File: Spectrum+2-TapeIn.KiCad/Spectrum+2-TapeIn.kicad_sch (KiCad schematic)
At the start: 15 parts, among them U1 LM358

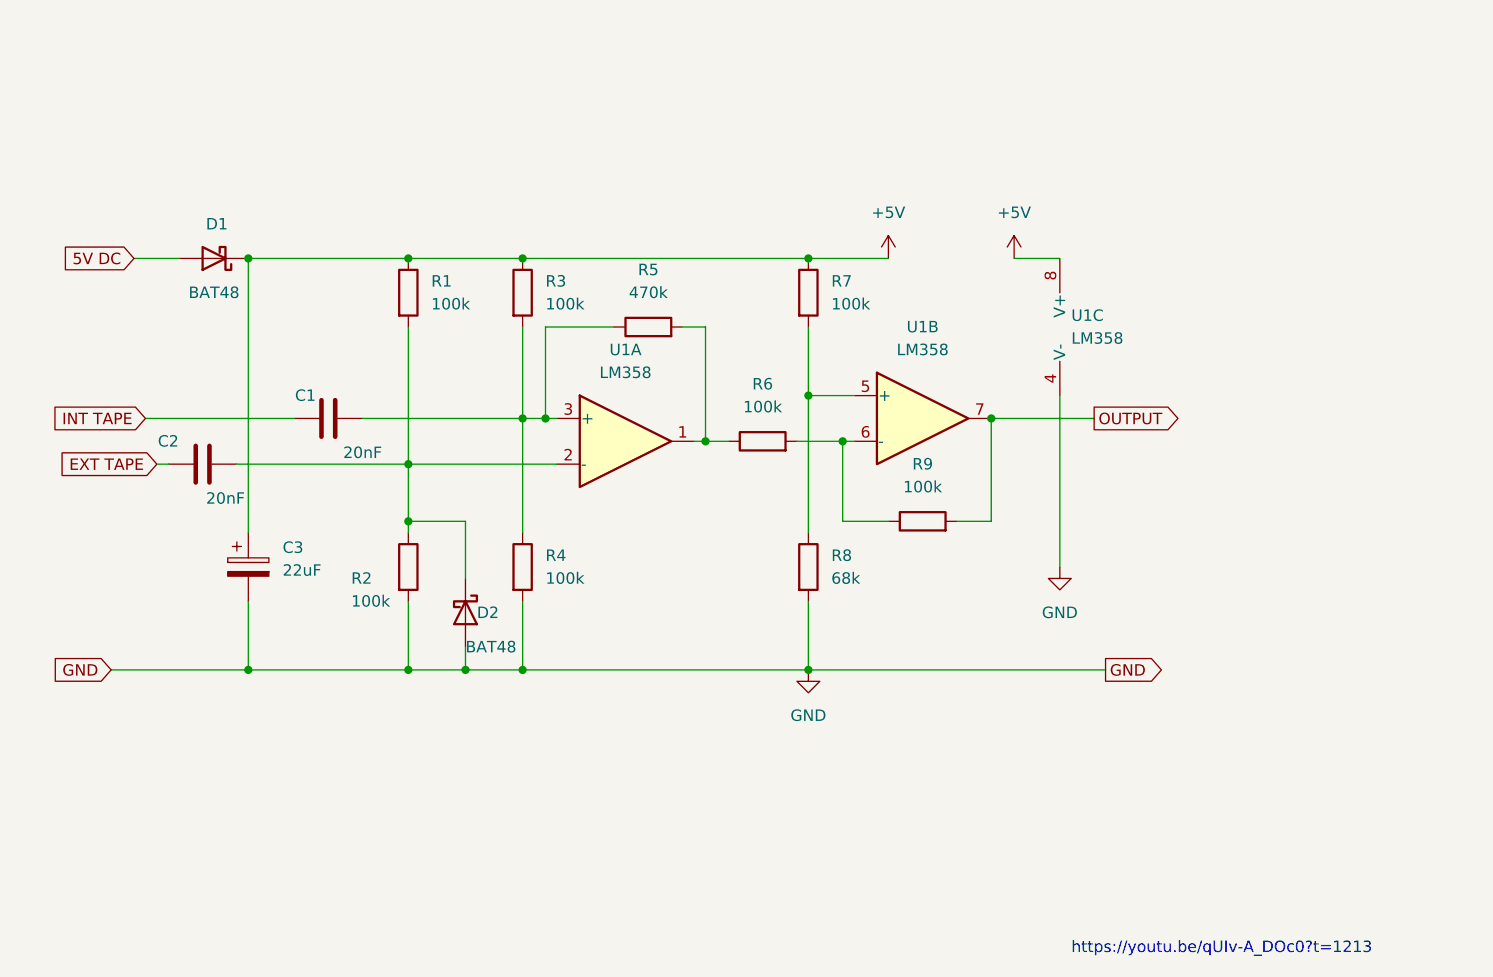
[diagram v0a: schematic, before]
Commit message: Rev. D
Proper connector for deck plug (no need to cut the wires).
Improved silkscreen, makes it easier to place components when building.
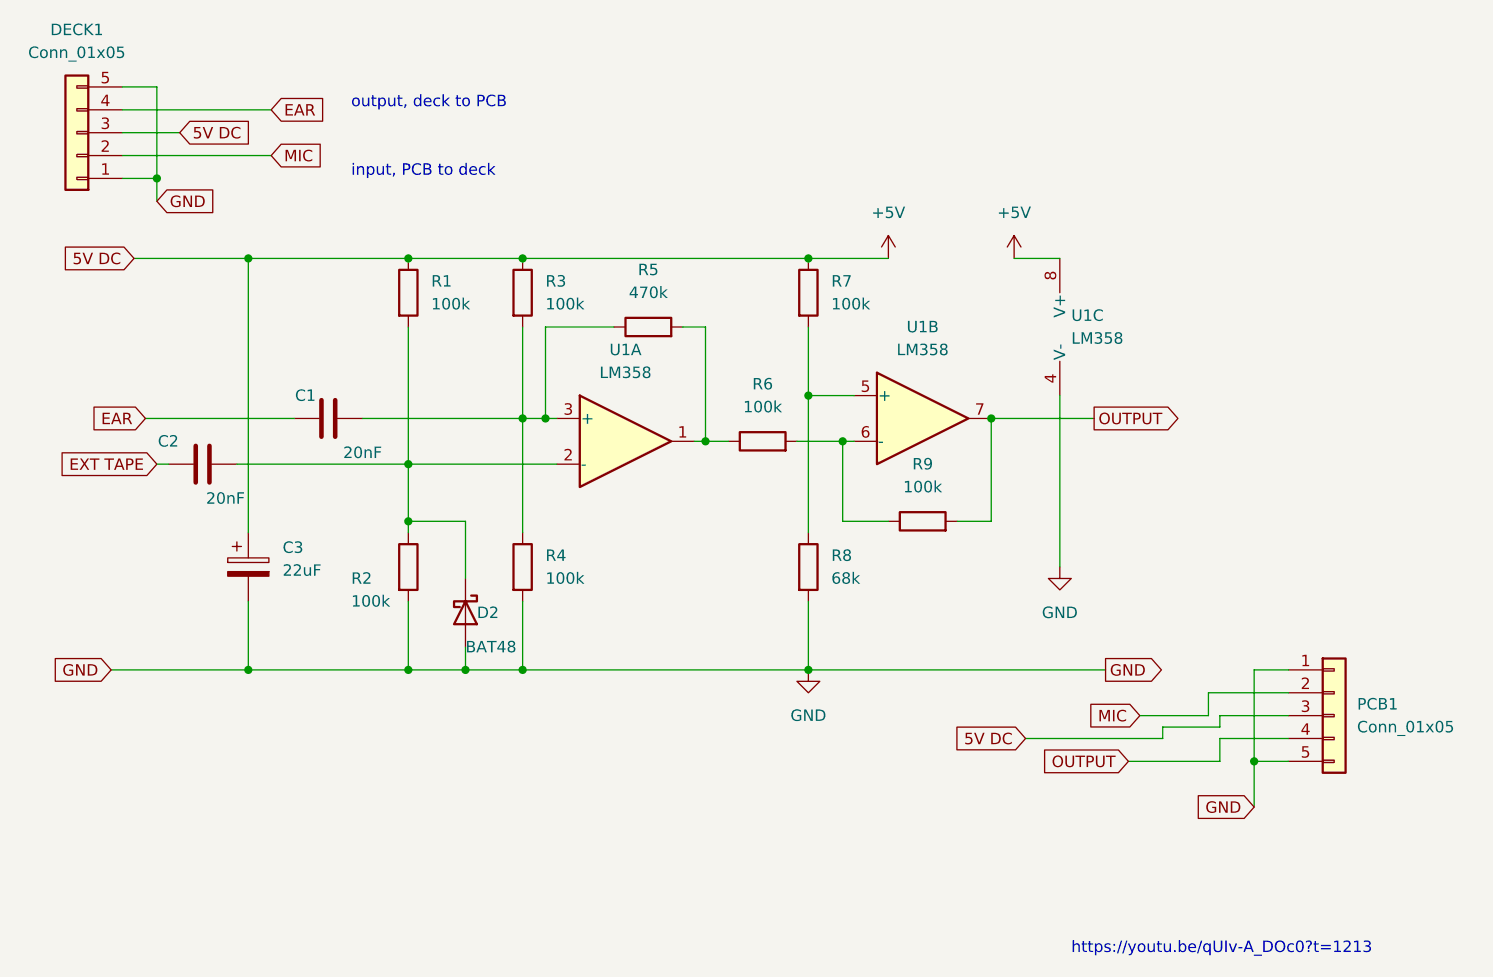
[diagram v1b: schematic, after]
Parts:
- removed D1: BAT48, Diode_THT:D_A-405_P7.62mm_Horizontal, symbol Device:D_Schottky
- added DECK1: Conn_01x05, Connector_Molex:Molex_KK-254_AE-6410-05A_1x05_P2.54mm_Vertical, symbol Connector_Generic:Conn_01x05
- added PCB1: Conn_01x05, Connector_Molex:Molex_KK-254_AE-6410-06A_1x05_P2.54mm_Vertical, symbol Connector_Generic:Conn_01x05
- D2: footprint Diode_THT:D_A-405_P7.62mm_Horizontal -> Diode_THT:D_A-405_P10.16mm_Horizontal
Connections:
- net +5V: now also DECK1.3 (Pin_3), PCB1.3 (Pin_3)
- net GND: now also DECK1.1 (Pin_1), DECK1.5 (Pin_5), PCB1.1 (Pin_1), PCB1.5 (Pin_5)
- net OUTPUT: now also PCB1.4 (Pin_4)
- net INT TAPE renamed EAR
- net EAR: now also DECK1.4 (Pin_4)
- new net MIC: DECK1.2 (Pin_2), PCB1.2 (Pin_2)
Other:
- note added: "input, PCB to deck"
- note added: "output, deck to PCB"
